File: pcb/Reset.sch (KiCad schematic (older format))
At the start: 6 parts, among them Q3 Q_NMOS_DGS, Q4 Q_NMOS_DGS, SW1 SW_PUSH

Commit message: v3 of f3fc. Correct mosfet pinout. Add measurement points. Remove MPU. Tweaked pinout with one less SPI.
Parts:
- removed Q3, Q4: Q_NMOS_DGS, Housings_SOT-23_SOT-143_TSOT-6:SOT-23_Handsoldering, symbol Q_NMOS_DGS
- added P6: RESET, Measurement_Points:Measurement_Point_Round-SMD-Pad_Small, symbol CONN_01X01
- added P7: BOOT0, Measurement_Points:Measurement_Point_Round-SMD-Pad_Small, symbol CONN_01X01
- added Q3, Q4: Q_NMOS_GSD, Housings_SOT-23_SOT-143_TSOT-6:SOT-23_Handsoldering, symbol Q_NMOS_GSD
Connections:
- wire segments 13 -> 14
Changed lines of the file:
@@
 LIBS:ti-regu
 LIBS:ti-power-mux
+LIBS:FlightController-cache
 EELAYER 25 0
 EELAYER END
@@
 $EndComp
 $Comp
-L GNDPWR #PWR045
+L GNDPWR #PWR038
 U 1 1 5615B692
 P 4800 4550
-F 0 "#PWR045" H 4800 4350 50  0001 C CNN
+F 0 "#PWR038" H 4800 4350 50  0001 C CNN
 F 1 "GNDPWR" H 4800 4420 50  0000 C CNN
 F 2 "" H 4800 4500 60  0000 C CNN
@@
 BOOT0
 $Comp
-L GNDPWR #PWR046
+L GNDPWR #PWR039
 U 1 1 56161C45
 P 6950 4400
-F 0 "#PWR046" H 6950 4200 50  0001 C CNN
+F 0 "#PWR039" H 6950 4200 50  0001 C CNN
 F 1 "GNDPWR" H 6950 4270 50  0000 C CNN
 F 2 "" H 6950 4350 60  0000 C CNN
@@
 $EndComp
 $Comp
-L GNDPWR #PWR047
+L GNDPWR #PWR040
 U 1 1 56161C6E
 P 6000 4400
-F 0 "#PWR047" H 6000 4200 50  0001 C CNN
+F 0 "#PWR040" H 6000 4200 50  0001 C CNN
 F 1 "GNDPWR" H 6000 4270 50  0000 C CNN
 F 2 "" H 6000 4350 60  0000 C CNN
@@
 	4800 3900 4800 4550
 Wire Wire Line
-	5400 3900 5400 4550
+	5400 3650 5400 4550
 Wire Wire Line
 	6600 3550 7300 3550
@@
 Wire Wire Line
 	6000 4100 6000 4400
-$Comp
-L Q_NMOS_DGS Q4
-U 1 1 56161A20
-P 7500 3550
-F 0 "Q4" H 7800 3600 50  0000 R CNN
-F 1 "Q_NMOS_DGS" H 8150 3500 50  0000 R CNN
-F 2 "Housings_SOT-23_SOT-143_TSOT-6:SOT-23_Handsoldering" H 7700 3650 29  0001 C CNN
-F 3 "" H 7500 3550 60  0000 C CNN
-	1    7500 3550
-	1    0    0    -1
-$EndComp
-$Comp
-L Q_NMOS_DGS Q3
-U 1 1 561619DC
-P 5900 3900
-F 0 "Q3" H 6200 3950 50  0000 R CNN
-F 1 "Q_NMOS_DGS" H 6550 3850 50  0000 R CNN
-F 2 "Housings_SOT-23_SOT-143_TSOT-6:SOT-23_Handsoldering" H 6100 4000 29  0001 C CNN
-F 3 "" H 5900 3900 60  0000 C CNN
-	1    5900 3900
-	1    0    0    -1
-$EndComp
 Text Notes 5500 4900 0    60   ~ 0
 Internally Pulled High
@@
 Pulled Low
 $Comp
-L VDD #PWR048
+L VDD #PWR041
 U 1 1 563D51E3
 P 7600 2950
-F 0 "#PWR048" H 7600 2800 50  0001 C CNN
+F 0 "#PWR041" H 7600 2800 50  0001 C CNN
 F 1 "VDD" H 7600 3100 50  0000 C CNN
 F 2 "" H 7600 2950 60  0000 C CNN
@@
 $EndComp
 $Comp
-L VDD #PWR049
+L VDD #PWR042
 U 1 1 563D5246
 P 6000 2950
-F 0 "#PWR049" H 6000 2800 50  0001 C CNN
+F 0 "#PWR042" H 6000 2800 50  0001 C CNN
 F 1 "VDD" H 6000 3100 50  0000 C CNN
 F 2 "" H 6000 2950 60  0000 C CNN
@@
 Wire Wire Line
 	6000 3100 6000 2950
+$Comp
+L Q_NMOS_GSD Q3
+U 1 1 5654B19F
+P 5900 3900
+F 0 "Q3" H 6200 3950 50  0000 R CNN
+F 1 "Q_NMOS_GSD" H 6550 3850 50  0000 R CNN
+F 2 "Housings_SOT-23_SOT-143_TSOT-6:SOT-23_Handsoldering" H 6100 4000 29  0001 C CNN
+F 3 "" H 5900 3900 60  0000 C CNN
+	1    5900 3900
+	1    0    0    -1
+$EndComp
+$Comp
+L Q_NMOS_GSD Q4
+U 1 1 5654B200
+P 7500 3550
+F 0 "Q4" H 7800 3600 50  0000 R CNN
+F 1 "Q_NMOS_GSD" H 8150 3500 50  0000 R CNN
+F 2 "Housings_SOT-23_SOT-143_TSOT-6:SOT-23_Handsoldering" H 7700 3650 29  0001 C CNN
+F 3 "" H 7500 3550 60  0000 C CNN
+	1    7500 3550
+	1    0    0    -1
+$EndComp
+$Comp
+L CONN_01X01 P6
+U 1 1 56554BA3
+P 5400 3450
+F 0 "P6" H 5400 3550 50  0000 C CNN
+F 1 "RESET" V 5500 3450 50  0000 C CNN
+F 2 "Measurement_Points:Measurement_Point_Round-SMD-Pad_Small" H 5400 3450 60  0001 C CNN
+F 3 "" H 5400 3450 60  0000 C CNN
+	1    5400 3450
+	0    -1   -1   0
+$EndComp
+Connection ~ 5400 3900
+$Comp
+L CONN_01X01 P7
+U 1 1 56554C77
+P 8050 4050
+F 0 "P7" H 8050 4150 50  0000 C CNN
+F 1 "BOOT0" H 8250 4050 50  0000 C CNN
+F 2 "Measurement_Points:Measurement_Point_Round-SMD-Pad_Small" H 8050 4050 60  0001 C CNN
+F 3 "" H 8050 4050 60  0000 C CNN
+	1    8050 4050
+	1    0    0    -1
+$EndComp
+Wire Wire Line
+	7850 4050 7600 4050
+Connection ~ 7600 4050
 $EndSCHEMATC

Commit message: F3FC v6 which features correct reset circuitry.
Also:
* Routes USB as differential pair.
* Corrects reset circuit.
* Adds fiducials
* Matches up LED numbering to reference
* Supports current pin from power connector.
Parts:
- added Q1: Q_PMOS_GSD, TO_SOT_Packages_SMD:SOT-23, symbol Q_PMOS_GSD
- added R7: 10k, Resistors_SMD:R_0603_HandSoldering, symbol R
- Q3, Q4: footprint Housings_SOT-23_SOT-143_TSOT-6:SOT-23_Handsoldering -> TO_SOT_Packages_SMD:SOT-23
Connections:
- wire segments 14 -> 15
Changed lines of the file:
@@
 	0    1    1    0
 $EndComp
-Text HLabel 7750 4400 2    60   Input ~ 0
+Text HLabel 8700 3850 2    60   Input ~ 0
 BOOT0
 $Comp
@@
 	7600 2950 7600 3350
 Wire Wire Line
-	7600 3750 7600 4400
+	8550 3200 8550 3850
 Wire Wire Line
 	6950 3950 6950 4400
@@
 Internally Pulled High
 Wire Wire Line
-	7600 4400 7750 4400
-Text Notes 7750 4550 0    60   ~ 0
+	8550 3850 8700 3850
+Text Notes 8700 4000 0    60   ~ 0
 Pulled Low
 $Comp
 L VDD #PWR044
 U 1 1 563D51E3
-P 7600 2950
-F 0 "#PWR044" H 7600 2800 50  0001 C CNN
-F 1 "VDD" H 7600 3100 50  0000 C CNN
-F 2 "" H 7600 2950 60  0000 C CNN
-F 3 "" H 7600 2950 60  0000 C CNN
-	1    7600 2950
+P 7600 2650
+F 0 "#PWR044" H 7600 2500 50  0001 C CNN
+F 1 "VDD" H 7600 2800 50  0000 C CNN
+F 2 "" H 7600 2650 60  0000 C CNN
+F 3 "" H 7600 2650 60  0000 C CNN
+	1    7600 2650
 	1    0    0    -1
 $EndComp
@@
 F 0 "Q3" H 6200 3950 50  0000 R CNN
 F 1 "Q_NMOS_GSD" H 6550 3850 50  0000 R CNN
-F 2 "Housings_SOT-23_SOT-143_TSOT-6:SOT-23_Handsoldering" H 6100 4000 29  0001 C CNN
+F 2 "TO_SOT_Packages_SMD:SOT-23" H 6100 4000 29  0001 C CNN
 F 3 "" H 5900 3900 60  0000 C CNN
 	1    5900 3900
@@
 F 0 "Q4" H 7800 3600 50  0000 R CNN
 F 1 "Q_NMOS_GSD" H 8150 3500 50  0000 R CNN
-F 2 "Housings_SOT-23_SOT-143_TSOT-6:SOT-23_Handsoldering" H 7700 3650 29  0001 C CNN
+F 2 "TO_SOT_Packages_SMD:SOT-23" H 7700 3650 29  0001 C CNN
 F 3 "" H 7500 3550 60  0000 C CNN
 	1    7500 3550
@@
 L CONN_01X01 P7
 U 1 1 56554C77
-P 8050 4050
-F 0 "P7" H 8050 4150 50  0000 C CNN
-F 1 "BOOT0" H 8250 4050 50  0000 C CNN
-F 2 "Measurement_Points:Measurement_Point_Round-SMD-Pad_Small" H 8050 4050 60  0001 C CNN
-F 3 "" H 8050 4050 60  0000 C CNN
-	1    8050 4050
+P 9000 3500
+F 0 "P7" H 9000 3600 50  0000 C CNN
+F 1 "BOOT0" H 9200 3500 50  0000 C CNN
+F 2 "Measurement_Points:Measurement_Point_Round-SMD-Pad_Small" H 9000 3500 60  0001 C CNN
+F 3 "" H 9000 3500 60  0000 C CNN
+	1    9000 3500
 	1    0    0    -1
 $EndComp
 Wire Wire Line
-	7850 4050 7600 4050
-Connection ~ 7600 4050
+	8800 3500 8550 3500
+Connection ~ 8550 3500
+$Comp
+L Q_PMOS_GSD Q1
+U 1 1 56C79F95
+P 8450 3000
+F 0 "Q1" H 8750 3050 50  0000 R CNN
+F 1 "Q_PMOS_GSD" H 9100 2950 50  0000 R CNN
+F 2 "TO_SOT_Packages_SMD:SOT-23" H 8650 3100 50  0001 C CNN
+F 3 "" H 8450 3000 50  0000 C CNN
+	1    8450 3000
+	1    0    0    -1
+$EndComp
+$Comp
+L VDD #PWR046
+U 1 1 56C79FCA
+P 8550 2800
+F 0 "#PWR046" H 8550 2650 50  0001 C CNN
+F 1 "VDD" H 8550 2950 50  0000 C CNN
+F 2 "" H 8550 2800 60  0000 C CNN
+F 3 "" H 8550 2800 60  0000 C CNN
+	1    8550 2800
+	1    0    0    -1
+$EndComp
+$Comp
+L GNDPWR #PWR047
+U 1 1 56C7A03D
+P 7600 3750
+F 0 "#PWR047" H 7600 3550 50  0001 C CNN
+F 1 "GNDPWR" H 7600 3620 50  0000 C CNN
+F 2 "" H 7600 3700 60  0000 C CNN
+F 3 "" H 7600 3700 60  0000 C CNN
+	1    7600 3750
+	1    0    0    -1
+$EndComp
+$Comp
+L R R7
+U 1 1 56C7A063
+P 7600 2800
+F 0 "R7" V 7680 2800 50  0000 C CNN
+F 1 "10k" V 7600 2800 50  0000 C CNN
+F 2 "Resistors_SMD:R_0603_HandSoldering" V 7530 2800 30  0001 C CNN
+F 3 "" H 7600 2800 30  0000 C CNN
+	1    7600 2800
+	1    0    0    -1
+$EndComp
+Wire Wire Line
+	8250 3000 7600 3000
+Connection ~ 7600 3000
 $EndSCHEMATC

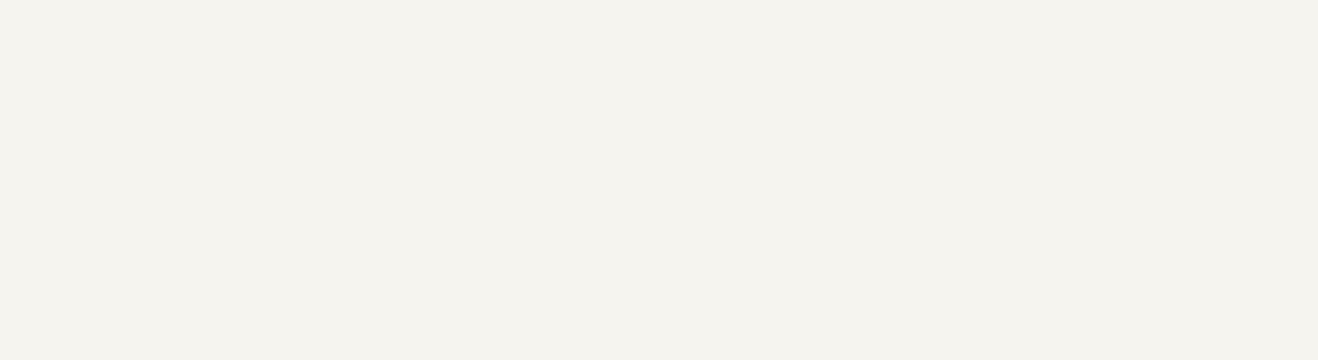
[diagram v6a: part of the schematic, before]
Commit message: Add license information to many files. PCB design files are CC-BY and code is MIT license.
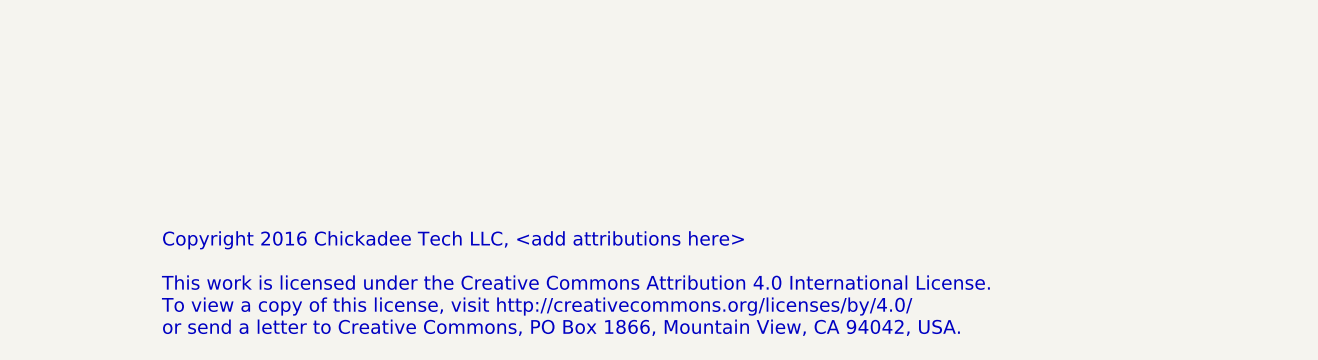
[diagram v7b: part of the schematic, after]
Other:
- note added: "Copyright 2016 Chickadee Tech LLC, <add attributions here>\n\nThis work is licensed under the Creative Commons Attribution 4.0 International License.\nTo view a copy of this license, visit http://creativecommons.org/licenses/by/4.0/\nor send a letter to Creative Commons, PO Box 1866, Mountain View, CA 94042, USA."
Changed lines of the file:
@@
 	8250 3000 7600 3000
 Connection ~ 7600 3000
+Text Notes 7050 7050 0    60   ~ 0
+Copyright 2016 Chickadee Tech LLC, <add attributions here>\n\nThis work is licensed under the Creative Commons Attribution 4.0 International License.\nTo view a copy of this license, visit http://creativecommons.org/licenses/by/4.0/\nor send a letter to Creative Commons, PO Box 1866, Mountain View, CA 94042, USA.
 $EndSCHEMATC
